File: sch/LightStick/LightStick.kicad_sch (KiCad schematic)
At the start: 19 parts, among them J1 +BATT, J2 GND, Q1 IRLML0030, Q2 IRLML0030, Q3 IRLML0030, Q4 IRLML0030, SW1 SW_Push, SW2 SW_Push, U2 XIAO-nRF54l15-SMD

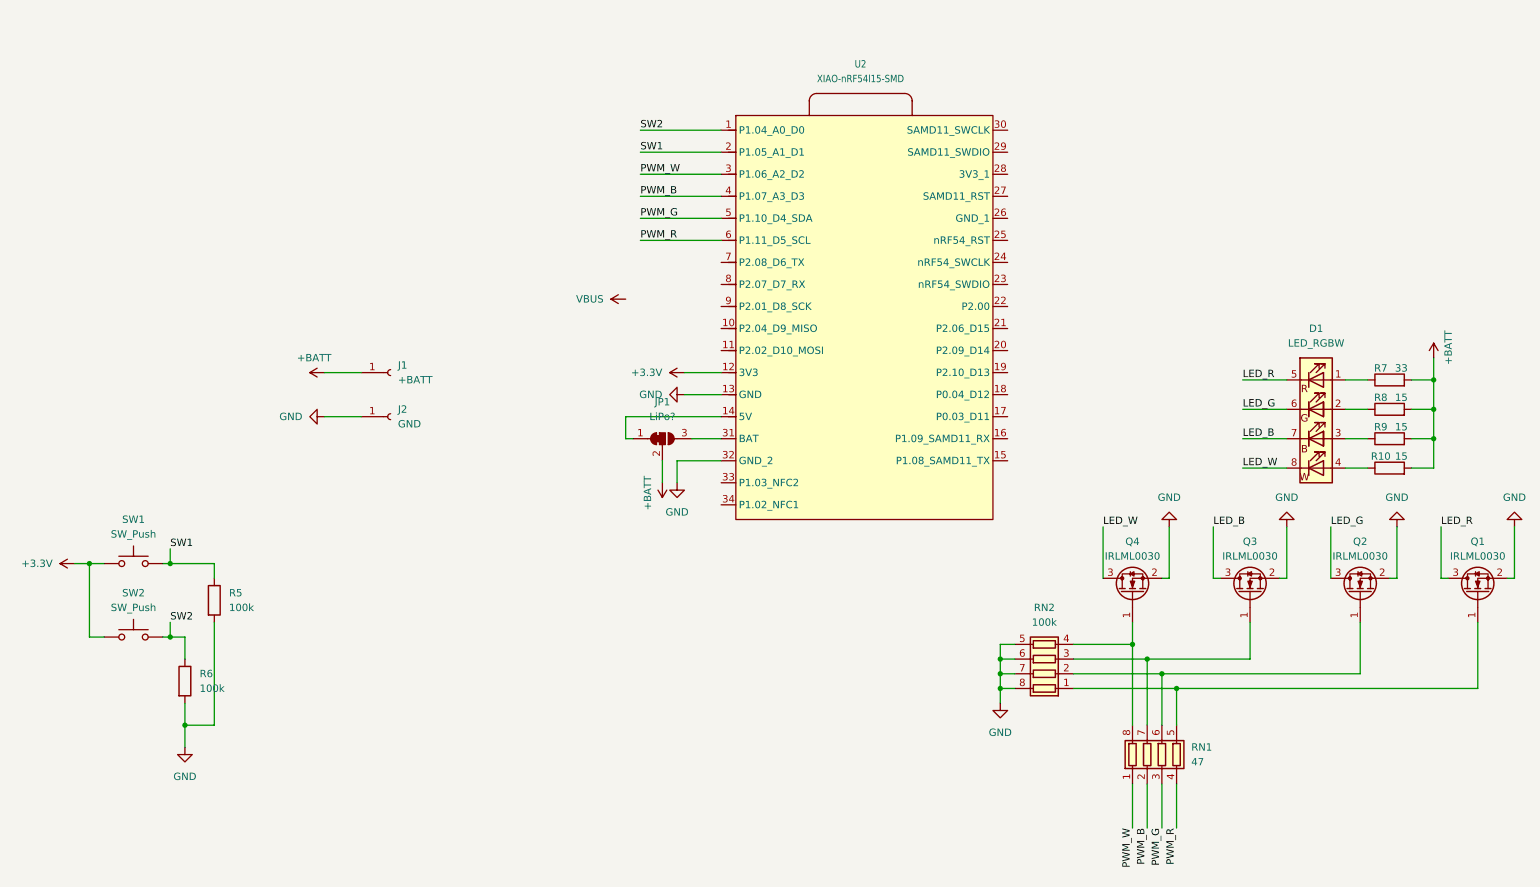
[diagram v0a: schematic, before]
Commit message: Raytac Module version
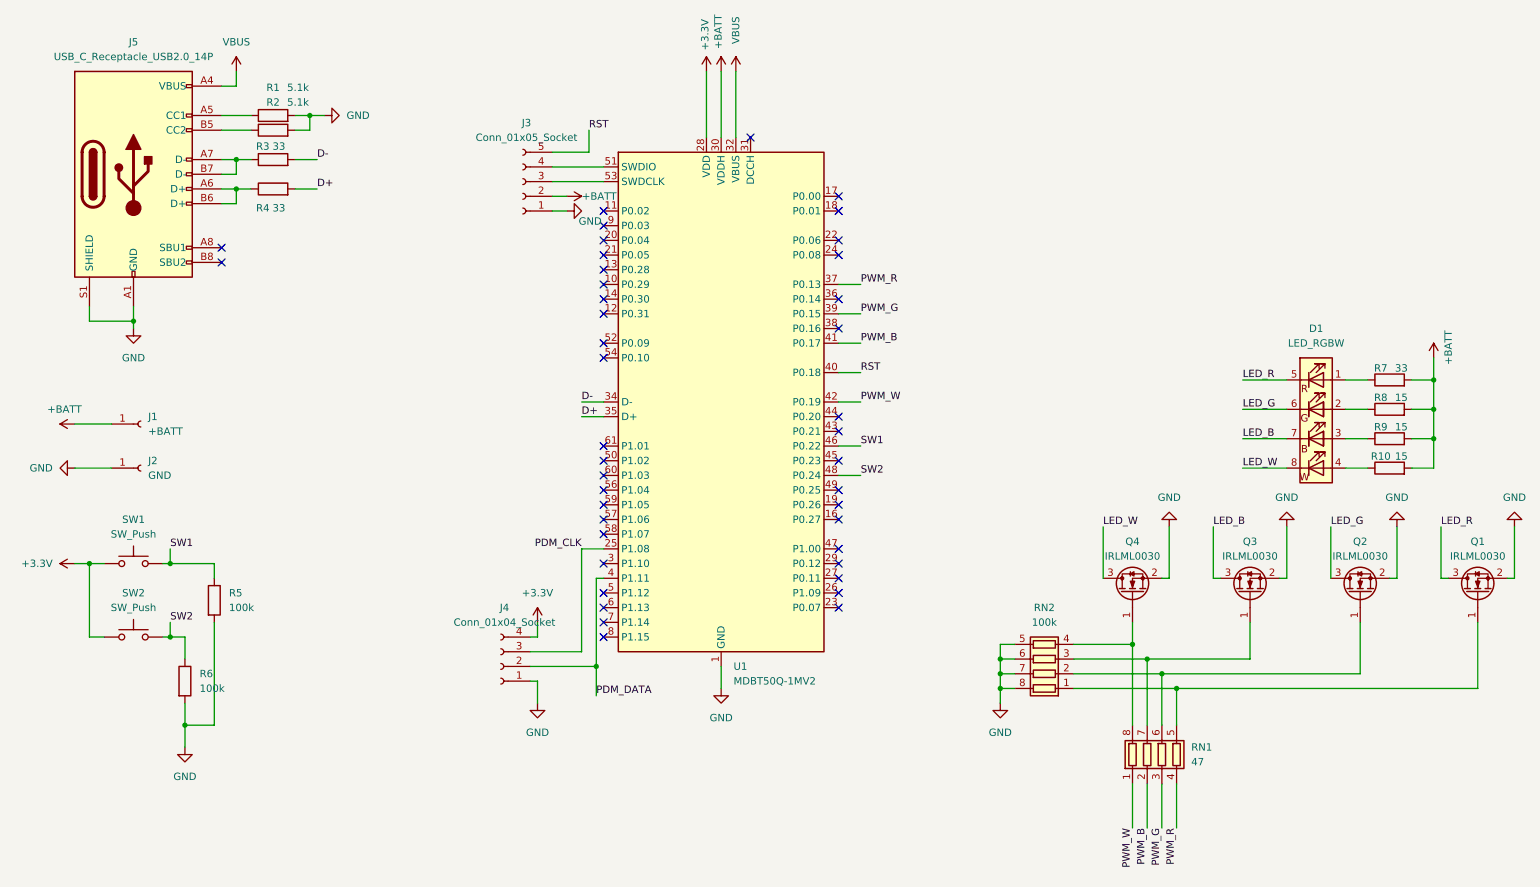
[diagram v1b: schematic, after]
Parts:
- removed JP1: LiPo?, Jumper:SolderJumper-3_P1.3mm_Bridged12_RoundedPad1.0x1.5mm, symbol Jumper:SolderJumper_3_Bridged12
- removed U2: XIAO-nRF54l15-SMD, parts:XIAO-nRF54l15-SMD, symbol Seeed_Studio_XIAO_Series:XIAO-nRF54l15-SMD
- added J3: Conn_01x05_Socket, Connector_JST:JST_SH_SM05B-SRSS-TB_1x05-1MP_P1.00mm_Horizontal, symbol Connector:Conn_01x05_Socket
- added J4: Conn_01x04_Socket, Connector_JST:JST_SH_SM04B-SRSS-TB_1x04-1MP_P1.00mm_Horizontal, symbol Connector:Conn_01x04_Socket
- added J5: USB_C_Receptacle_USB2.0_14P, Connector_USB:USB_C_Receptacle_Palconn_UTC16-G, symbol Connector:USB_C_Receptacle_USB2.0_16P
- added R1, R2: 5.1k, Resistor_SMD:R_0603_1608Metric_Pad0.98x0.95mm_HandSolder, symbol Device:R
- added R3, R4: 33, Resistor_SMD:R_0603_1608Metric_Pad0.98x0.95mm_HandSolder, symbol Device:R
- added U1: MDBT50Q-1MV2, RF_Module:Raytac_MDBT50Q, symbol RF_Module:MDBT50Q-1MV2
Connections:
- net +3.3V: now also J4.4 (Pin_4), U1.28 (VDD)
- net +BATT: now also J3.2 (Pin_2), U1.30 (VDDH)
- net GND: now also J3.1 (Pin_1), J4.1 (Pin_1), J5.A1 (GND), J5.A12 (GND), J5.B1 (GND), J5.B12 (GND), J5.S1 (SHIELD), R1.2, R2.2, U1.1 (GND), U1.15 (GND), U1.2 (GND), U1.33 (GND), U1.55 (GND)
- net PWM_B: now also U1.41 (P0.17)
- net PWM_G: now also U1.39 (P0.15)
- net PWM_R: now also U1.37 (P0.13)
- net PWM_W: now also U1.42 (P0.19)
- net SW1: now also U1.46 (P0.22)
- net SW2: now also U1.48 (P0.24)
- net VBUS: now also J5.A4 (VBUS), J5.A9 (VBUS), J5.B4 (VBUS), J5.B9 (VBUS), U1.32 (VBUS)
- new net: J5.B5 (CC2), R2.1
- new net: J5.A5 (CC1), R1.1
- new net: J5.A6 (D+), J5.B6 (D+), R4.1
- new net: J5.A7 (D-), J5.B7 (D-), R3.1
- new net: J3.4 (Pin_4), U1.51 (SWDIO)
- new net: J3.3 (Pin_3), U1.53 (SWDCLK)
- new net D+: R4.2, U1.35 (D+)
- new net D-: R3.2, U1.34 (D-)
- new net PDM_CLK: J4.3 (Pin_3), U1.25 (P1.08)
- new net PDM_DATA: J4.2 (Pin_2), U1.4 (P1.11)
- new net RST: J3.5 (Pin_5), U1.40 (P0.18)
- no-connect marks 0 -> 42
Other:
- moved on the sheet: J1, J2
